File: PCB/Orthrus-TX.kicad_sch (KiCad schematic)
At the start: 143 parts, among them J1 HRO-TYPE-C-31-M-13x, U2 SRV05-4, U3 SRV05-4, U4 SRV05-4, U5 SRV05-4, U6 SRV05-4, U7 SRV05-4, U8 SRV05-4

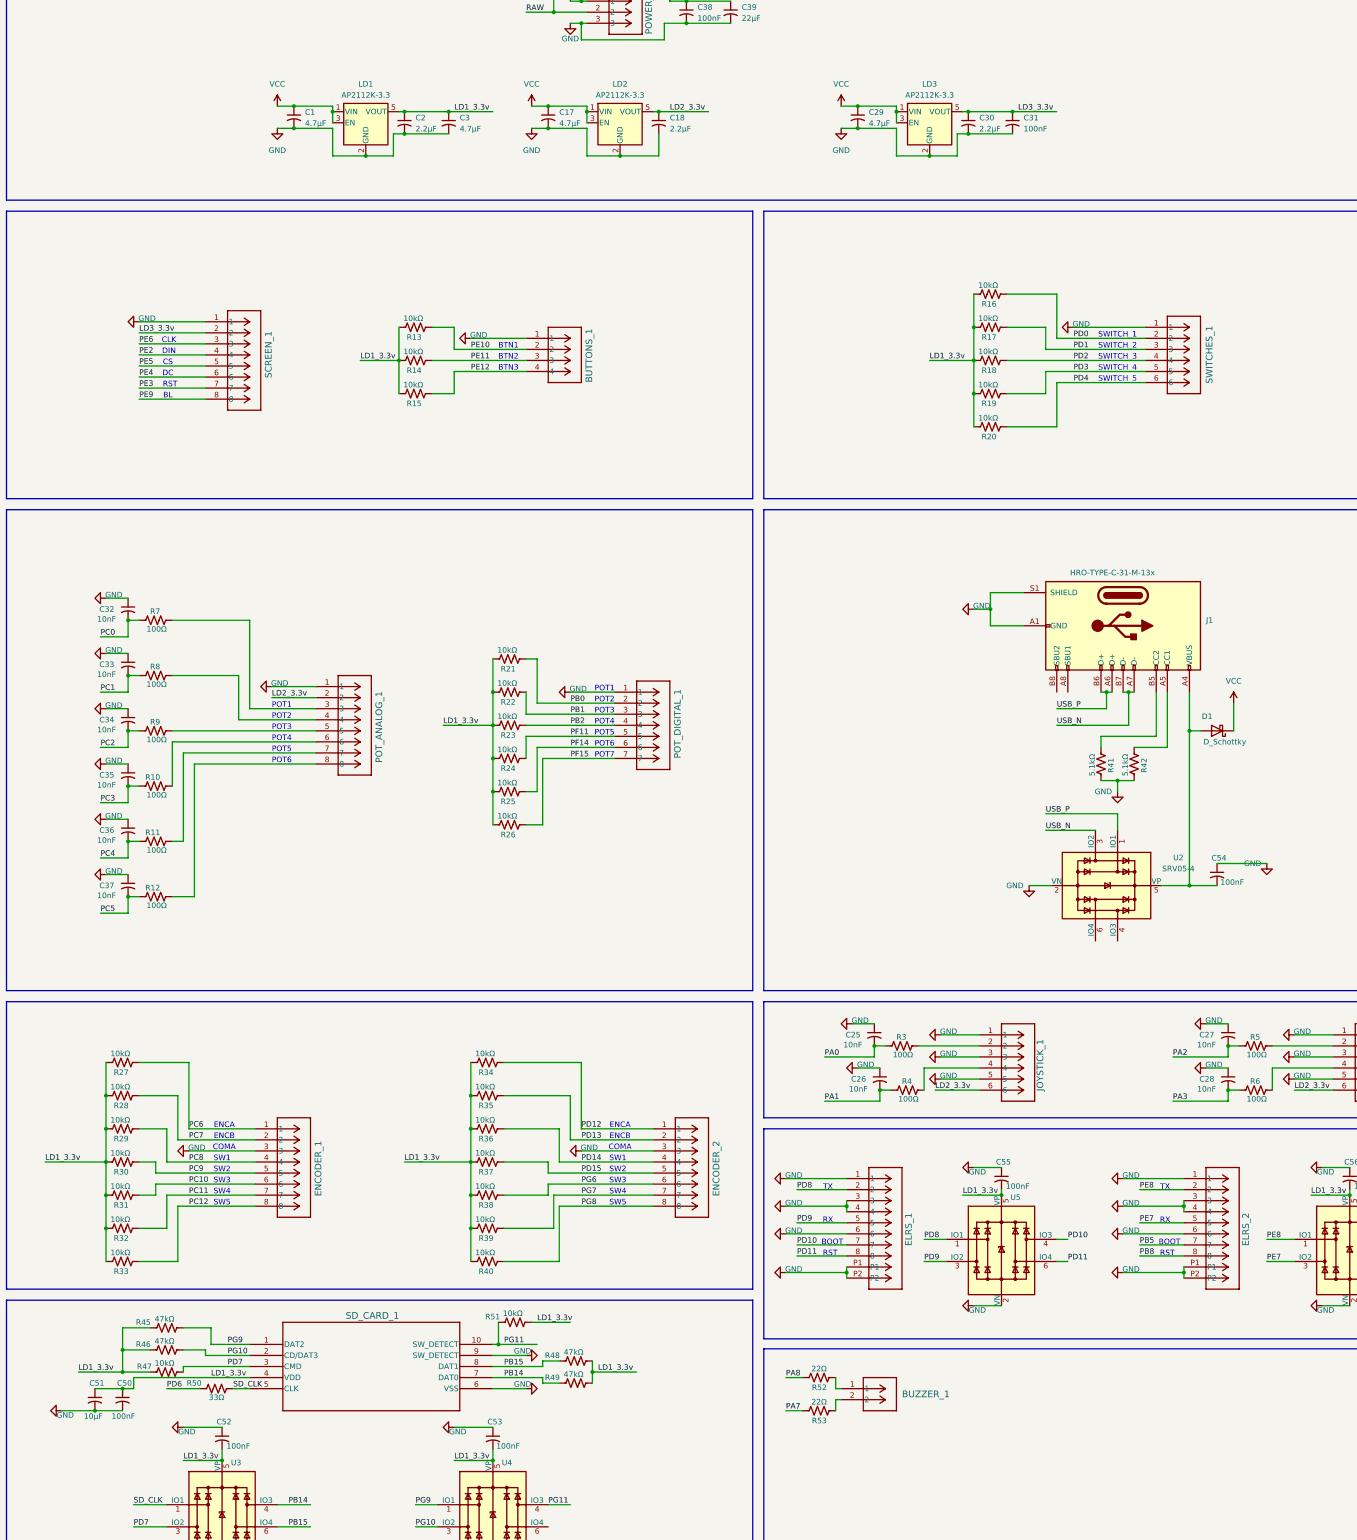
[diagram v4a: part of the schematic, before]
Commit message: extra LDO for the SDCard
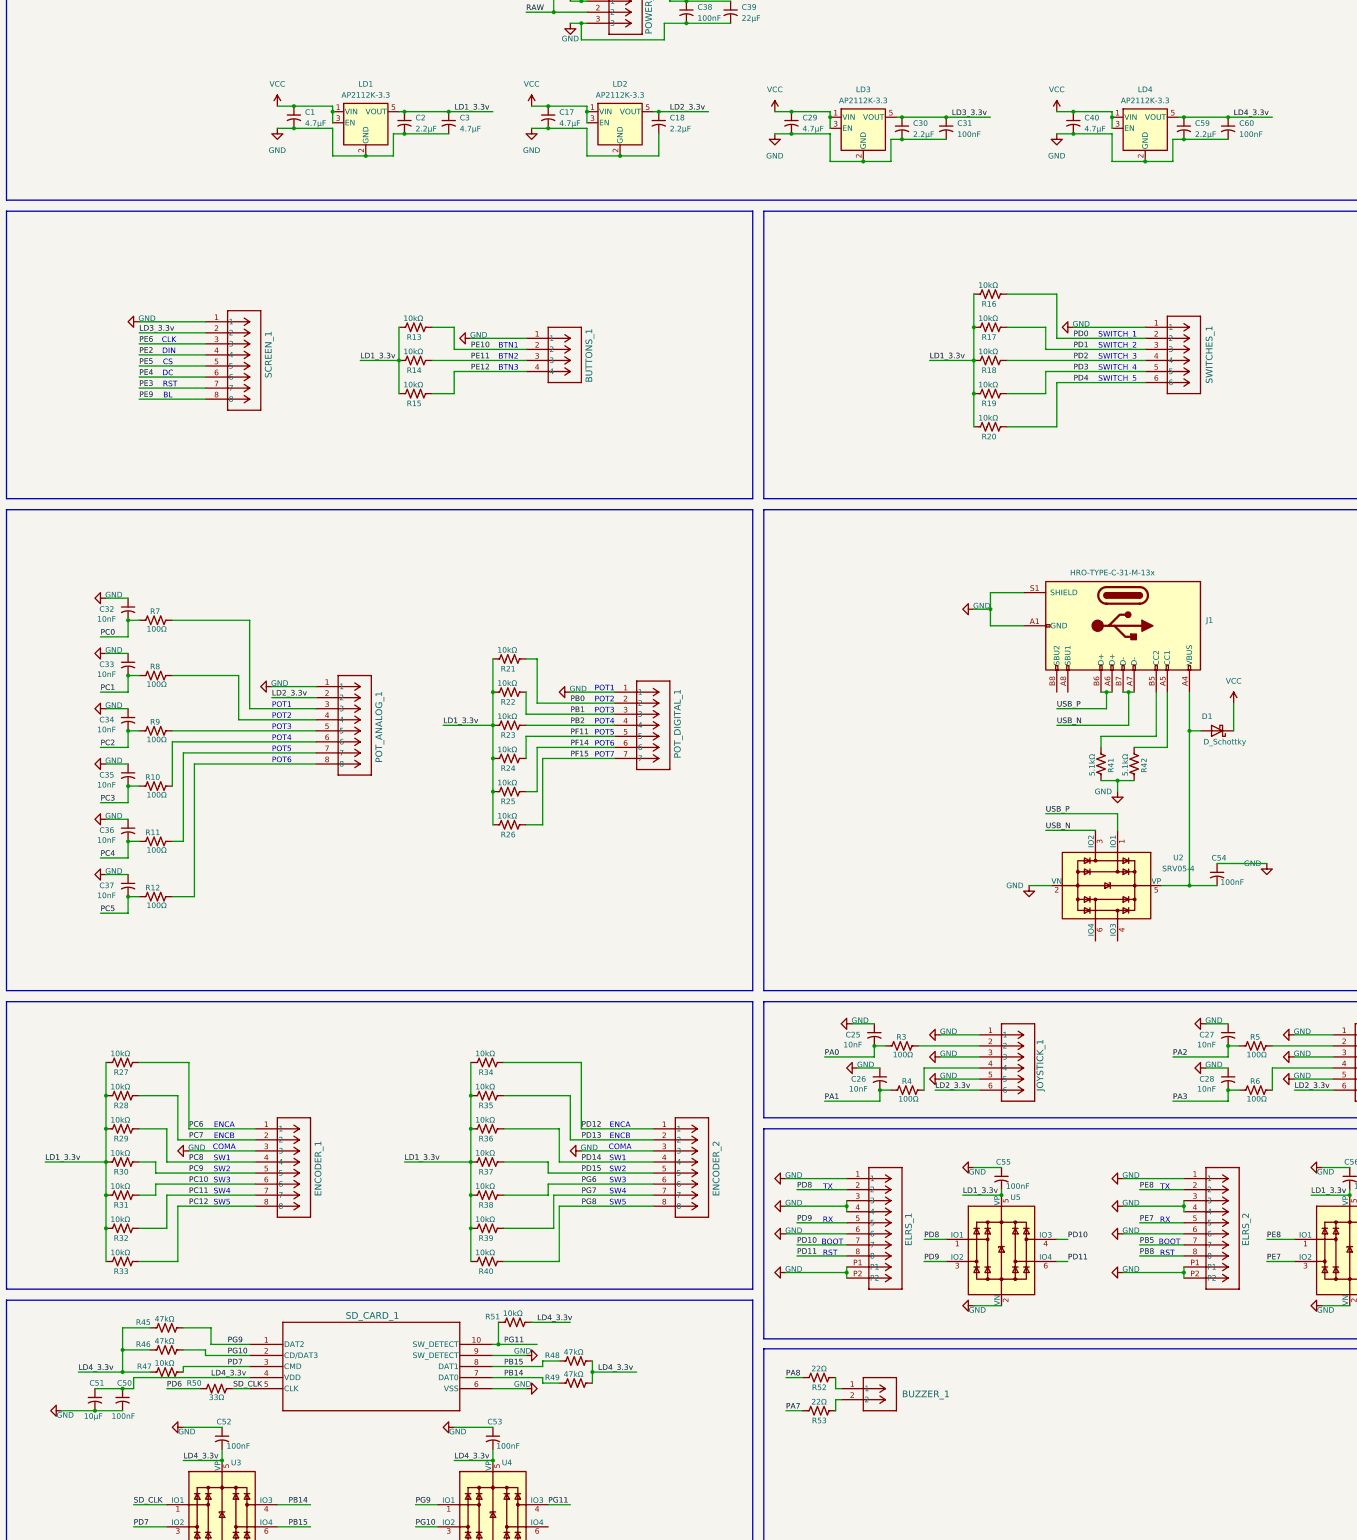
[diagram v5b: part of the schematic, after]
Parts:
- added C40: 4.7µF, Capacitor_SMD:C_0603_1608Metric, symbol Device:C_Small_US
- added C59: 2.2µF, Capacitor_SMD:C_0603_1608Metric, symbol Device:C_Small_US
- added C60: 100nF, Capacitor_SMD:C_0603_1608Metric, symbol Device:C_Small_US
- added LD4: AP2112K-3.3, Package_TO_SOT_SMD:SOT-23-5, symbol Regulator_Linear:AP2112K-3.3
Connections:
- net GND: now also C40.2, C59.2, C60.2, LD4.2 (GND)
- net LD1_3.3v: no longer C50.1, C51.1, C52.2, C53.2, R45.2, R46.2, R47.2, R48.1, R49.1, R51.1, SD_CARD_1.4 (VDD), U3.5 (VP), U4.5 (VP)
- net VCC: now also C40.1, LD4.1 (VIN), LD4.3 (EN)
- new net LD4_3.3v: C50.1, C51.1, C52.2, C53.2, C59.1, C60.1, LD4.5 (VOUT), R45.2, R46.2, R47.2, R48.1, R49.1, R51.1, SD_CARD_1.4 (VDD), U3.5 (VP), U4.5 (VP)
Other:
- moved on the sheet: C29, C30, C31, LD3

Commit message: DRC
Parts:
- added C61: 220pF, Capacitor_SMD:C_0603_1608Metric, symbol Device:C_Small_US
- C22: value 4.7µF -> 10µF
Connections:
- net GND: now also C61.1
- net VLXSMPS: now also C61.2
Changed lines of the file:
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@@
 	(wire
 		(pts
+			(xy 424.18 69.85) (xy 424.18 66.04)
+		)
+		(stroke
+			(width 0)
+			(type default)
+		)
+	)
+	(wire
+		(pts
 			(xy 285.75 245.11) (xy 285.75 209.55)
 		)
@@
 	(wire
 		(pts
+			(xy 424.18 66.04) (xy 417.83 66.04)
+		)
+		(stroke
+			(width 0)
+			(type default)
+		)
+	)
+	(wire
+		(pts
 			(xy 294.64 68.58) (xy 304.8 68.58)
 		)
@@
 	(wire
 		(pts
+			(xy 408.94 60.96) (xy 417.83 60.96)
+		)
+		(stroke
+			(width 0)
+			(type default)
+		)
+	)
+	(wire
+		(pts
 			(xy 54.61 214.63) (xy 85.09 214.63)
 		)
@@
 			)
 		)
-		(property "Value" "4.7µF"
+		(property "Value" "10µF"
 			(at 375.92 137.2869 0)
 			(show_name no)
@@
 	)
 	(symbol
+		(lib_id "Device:C_Small_US")
+		(at 417.83 63.5 0)
+		(unit 1)
+		(body_style 1)
+		(exclude_from_sim no)
+		(in_bom yes)
+		(on_board yes)
+		(in_pos_files yes)
+		(dnp no)
+		(property "Reference" "C61"
+			(at 410.21 62.23 0)
+			(show_name no)
+			(do_not_autoplace no)
+			(effects
+				(font
+					(size 1.27 1.27)
+				)
+				(justify left)
+			)
+		)
+		(property "Value" "220pF"
+			(at 410.21 64.516 0)
+			(show_name no)
+			(do_not_autoplace no)
+			(effects
+				(font
+					(size 1.27 1.27)
+				)
+				(justify left)
+			)
+		)
+		(property "Footprint" "Capacitor_SMD:C_0603_1608Metric"
+			(at 417.83 63.5 0)
+			(hide yes)
+			(show_name no)
+			(do_not_autoplace no)
+			(effects
+				(font
+					(size 1.27 1.27)
+				)
+			)
+		)
+		(property "Datasheet" ""
+			(at 417.83 63.5 0)
+			(hide yes)
+			(show_name no)
+			(do_not_autoplace no)
+			(effects
+				(font
+					(size 1.27 1.27)
+				)
+			)
+		)
+		(property "Description" "capacitor, small US symbol"
+			(at 417.83 63.5 0)
+			(hide yes)
+			(show_name no)
+			(do_not_autoplace no)
+			(effects
+				(font
+					(size 1.27 1.27)
+				)
+			)
+		)
+		(property "LCSC" ""
+			(at 417.83 63.5 0)
+			(hide yes)
+			(show_name no)
+			(do_not_autoplace no)
+			(effects
+				(font
+					(size 1.27 1.27)
+				)
+			)
+		)
+		(pin "2"
+		)
+		(pin "1"
+		)
+		(instances
+			(project "Orthrus-TX"
+				(path "/96e81b93-0369-470d-8547-b925c1f9f96d"
+					(reference "C61")
+					(unit 1)
+				)
+			)
+		)
+	)
+	(symbol
 		(lib_id "CONN_532610001-SD_08_MOL:532610871")
 		(at 59.69 115.57 0)
@@
 					(unit 1)
 				)
+			)
+		)
+	)
+	(symbol
+		(lib_id "power:GND")
+		(at 408.94 60.96 180)
+		(unit 1)
+		(body_style 1)
+		(exclude_from_sim no)
+		(in_bom yes)
+		(on_board yes)
+		(in_pos_files yes)
+		(dnp no)
+		(property "Reference" "#PWR078"
+			(at 408.94 54.61 0)
+			(hide yes)
+			(show_name no)
+			(do_not_autoplace no)
+			(effects
+				(font
+					(size 1.27 1.27)
+				)
+			)
+		)
+		(property "Value" "GND"
+			(at 405.13 58.928 0)
+			(show_name no)
+			(do_not_autoplace no)
+			(effects
+				(font
+					(size 1.27 1.27)
+				)
+			)
+		)
+		(property "Footprint" ""
+			(at 408.94 60.96 0)
+			(hide yes)
+			(show_name no)
+			(do_not_autoplace no)
+			(effects
+				(font
+					(size 1.27 1.27)
+				)
+			)
+		)
+		(property "Datasheet" ""
+			(at 408.94 60.96 0)
+			(hide yes)
+			(show_name no)
+			(do_not_autoplace no)
+			(effects
+				(font
+					(size 1.27 1.27)
+				)
+			)
+		)
+		(property "Description" "Power symbol creates a global label with name \"GND\" , ground"
+			(at 408.94 60.96 0)
+			(hide yes)
+			(show_name no)
+			(do_not_autoplace no)
+			(effects
+				(font
+					(size 1.27 1.27)
+				)
+			)
+		)
+		(pin "1"
+		)
+		(instances
+			(project "Orthrus-TX"
+				(path "/96e81b93-0369-470d-8547-b925c1f9f96d"
+					(reference "#PWR078")
+					(unit 1)
+				)

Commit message: pcb update
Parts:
- added C62: 100nF, Capacitor_SMD:C_0603_1608Metric, symbol Device:C_Small_US
- added R55: 1MΩ, Resistor_SMD:R_0603_1608Metric, symbol Device:R_US
- R54: value 22Ω -> 47Ω; LCSC C2907129 -> (none)
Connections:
- net GND: now also C62.1, R55.1; no longer J1.S1 (SHIELD)
- new net: C62.2, J1.S1 (SHIELD), R55.2

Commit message: pcb update
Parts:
- added FL1: 0603USB-601, Inductor_SMD:L_CommonModeChoke_Coilcraft_0603USB, symbol Filter:0603USB-601
- added R56: 100Ω, Resistor_SMD:R_0603_1608Metric, symbol Device:R_US
- added R57: 100kΩ, Resistor_SMD:R_0603_1608Metric, symbol Device:R_US
- added U1: AO3407A, SOT-23-3L_AOS, symbol SOT-23-3L_AOS:AO3407A
- C22: LCSC C19666 -> C19702
- C23, C24: value 12pF -> 33pF; LCSC C38523 -> C472790
- C61: LCSC (none) -> C882575
- R54: LCSC (none) -> C403245
- R55: LCSC (none) -> C491226
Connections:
- net GND: now also R57.2
- net PG11: now also R45.1, SD_CARD_1.1 (DAT2), U4.1 (IO1); no longer R51.2, SD_CARD_1.10 (SW_DETECT), U4.4 (IO3)
- net PH1: now also R56.2; no longer C24.1, XTAL1.3
- net USB_N: now also FL1.1; no longer STM32H745ZIT6.100 (PA11)
- net USB_P: now also FL1.4; no longer STM32H745ZIT6.101 (PA12)
- net VCC: now also U1.3 (D); no longer C38.1, C39.1, POWER_1.1
- net PG12: now reaches STM32H745ZIT6.125 (PG12)
- net PG12: now also R46.1, SD_CARD_1.2 (CD/DAT3), U4.3 (IO2)
- net PG13: now reaches STM32H745ZIT6.126 (PG13)
- net PG13: now also R51.2, SD_CARD_1.10 (SW_DETECT), U4.4 (IO3)
- removed net PG10: R46.1, SD_CARD_1.2 (CD/DAT3), STM32H745ZIT6.123 (PG10), U4.3 (IO2)
- removed net PG9: R45.1, SD_CARD_1.1 (DAT2), STM32H745ZIT6.122 (PG9), U4.1 (IO1)
- new net: R57.1, U1.2 (S)
- new net: C24.1, R56.1, XTAL1.3
- new net BATT_IN: C38.1, C39.1, POWER_1.1, U1.1 (G)
- new net USB_N_OUT: FL1.2, STM32H745ZIT6.100 (PA11)
- new net USB_P_OUT: FL1.3, STM32H745ZIT6.101 (PA12)
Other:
- moved on the sheet: C24, C54, U2
